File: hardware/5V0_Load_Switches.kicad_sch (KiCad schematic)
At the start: 28 parts, among them Q18 SI2302DDS-T1-GE3, Q19 SI2302DDS-T1-GE3, Q20 SI2302DDS-T1-GE3, U1 LMV321RIYLT, U2 INA199C1DCKR, U3 INA199C1DCKR, U4 INA199C1DCKR, U5 NVTFS5116PLTAG, U6 NVTFS5116PLTAG, U7 NVTFS5116PLTAG

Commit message: commit
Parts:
- R12, R13, R14: footprint (none) -> footprints:CRCW0603100KFKEAHP; symbol Device:R_US -> CRCW0603100KFKEAHP:CRCW0603100KFKEAHP; Arrow Part Number (none) -> CRCW0603100KFKEAHP; Arrow Price/Stock (none) -> https://www.arrow.com/en/products/crcw0603100kfkeahp/vishay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; Height (none) -> 0.55; Manufacturer_Name (none) -> Vishay; Manufacturer_Part_Number (none) -> CRCW0603100KFKEAHP; Mouser Part Number (none) -> 71-CRCW0603100KFKEAH; Mouser Price/Stock (none) -> https://www.mouser.co.uk/ProductDetail/Vishay-Dale/CRCW0603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
- R2: footprint (none) -> footprints:RC0805FR-0710KL; symbol Device:R_US -> RC0805FR-0710KL:RES
- R5: footprint (none) -> footprints:WSL2010R0200FEA; symbol Device:R_US -> WSL2010R0200FEA:WSL2010R0200FEA; Arrow Part Number (none) -> WSL2010R0200FEA; Arrow Price/Stock (none) -> https://www.arrow.com/en/products/wsl2010r0200fea/vishay; Manufacturer_Name (none) -> Vishay; Manufacturer_Part_Number (none) -> WSL2010R0200FEA; Mouser Part Number (none) -> 71-WSL2010R0200FEA; Mouser Price/Stock (none) -> https://www.mouser.co.uk/ProductDetail/Vishay-Dale/WSL2010R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
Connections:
- net +5V: now also R5.1; no longer R5.2
- net GND: now also R12.1, R13.1, R14.1; no longer R12.2, R13.2, R14.2, R2.1
- net at R1.1, U1.3 (+): no longer R2.2
- net at R8.1, U4.5 (IN-), U7.1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: now also R5.2; no longer R5.1
- net at Q20.1 (G), R10.2: now also R13.2; no longer R13.1
- net at Q18.1 (G), R11.2: now also R14.2; no longer R14.1
- net at Q19.1 (G), R9.2: now also R12.2; no longer R12.1
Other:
- moved on the sheet: R12, R13, R14, R2, R5

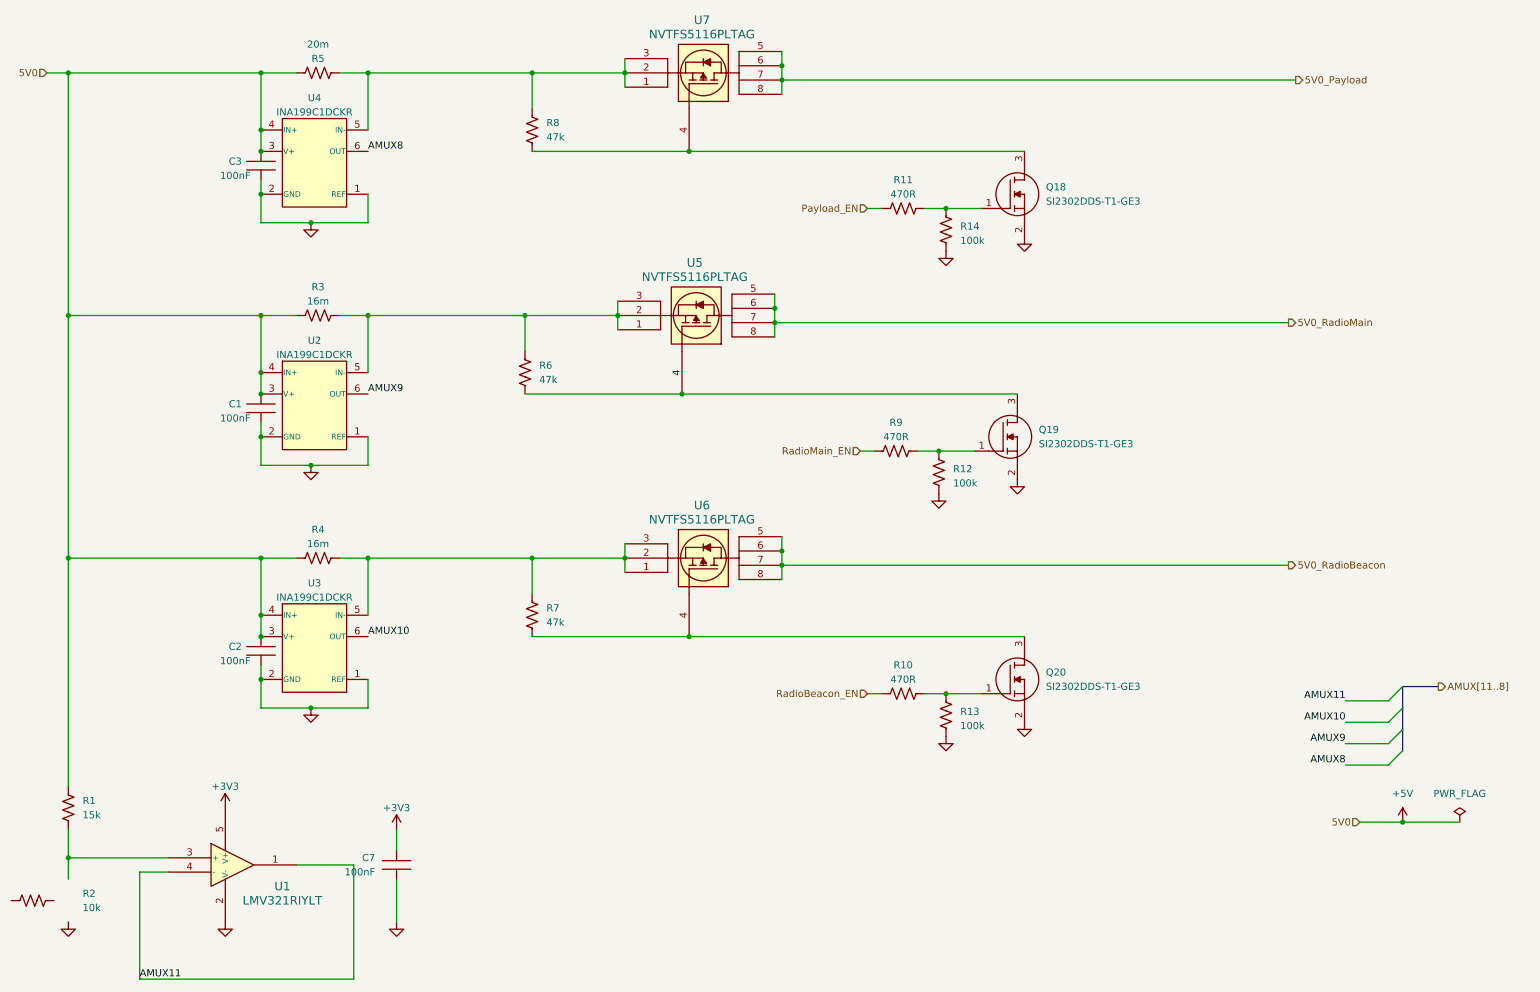
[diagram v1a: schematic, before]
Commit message: hardware: update in footprints
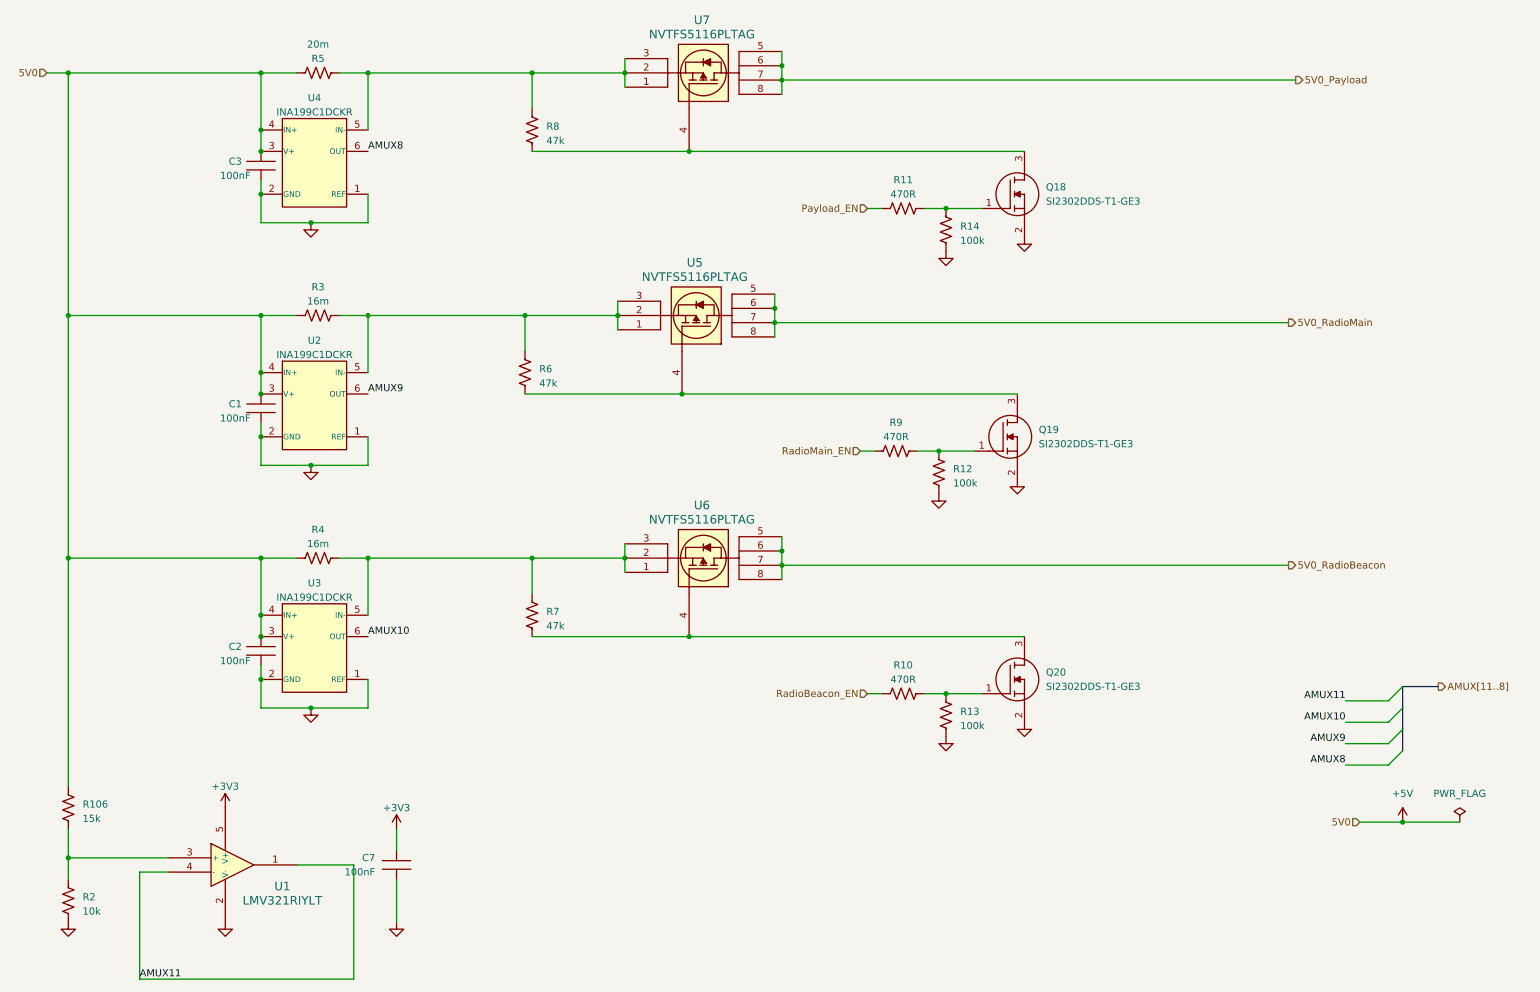
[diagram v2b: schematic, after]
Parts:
- removed R1: 15k, symbol Device:R_US
- added R106: 15k, footprints:CRCW060315K0FKEAHP, symbol CRCW060315K0FKEAHP:CRCW060315K0FKEAHP
- R10, R11, R9: footprint (none) -> footprints:CRCW0603470RFKEAHP; symbol Device:R_US -> CRCW0603470RFKEAHP:CRCW0603470RFKEAHP; automotive (none) -> Yes; automotive grade (none) -> Grade 0; category (none) -> Res; composition (none) -> Thick Film; device class L1 (none) -> Passive Components; device class L2 (none) -> Resistors; device class L3 (none) -> Chip SMD Resistors; height (none) -> 0.55mm; ipc land pattern name (none) -> RESC16085X45; lead free (none) -> Yes; library id (none) -> 3843bba7e74bf2ed; manufacturer (none) -> Vishay; package (none) -> 0603; power (none) -> 250mW; power rating (none) -> 0.33W; resistance (none) -> 470Ω; rohs (none) -> Yes; series (none) -> CRCW-HP e3; temperature coefficient (none) -> 100ppm/°C; temperature range high (none) -> +155°C; temperature range low (none) -> -55°C; tolerance (none) -> 1%; voltage rating (none) -> 75V
- R6, R7, R8: footprint (none) -> footprints:CRCW060347K0FKEAHP; symbol Device:R_US -> CRCW060347K0FKEAHP:CRCW060347K0FKEAHP; automotive (none) -> Yes; automotive grade (none) -> Grade 0; category (none) -> Res; composition (none) -> Thick Film; device class L1 (none) -> Passive Components; device class L2 (none) -> Resistors; device class L3 (none) -> Chip SMD Resistors; height (none) -> 0.55mm; ipc land pattern name (none) -> RESC16085X45; lead free (none) -> Yes; library id (none) -> 41c6336701360bfc; manufacturer (none) -> Vishay; package (none) -> 0603; power (none) -> 250mW; power rating (none) -> 0.33W; resistance (none) -> 47kΩ; rohs (none) -> Yes; series (none) -> CRCW-HP e3; temperature coefficient (none) -> 100ppm/°C; temperature range high (none) -> +155°C; temperature range low (none) -> -55°C; tolerance (none) -> 1%; voltage rating (none) -> 75V
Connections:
- net +5V: now also R106.2
- net GND: now also R2.2
- net Payload_EN: now also R11.2; no longer R11.1
- net RadioBeacon_EN: now also R10.2; no longer R10.1
- net RadioMain_EN: now also R9.2; no longer R9.1
- net at R4.1, U3.5 (IN-), U6.1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: now also R7.2; no longer R7.1
- net at Q20.3 (D), U6.4: now also R7.1; no longer R7.2
- net at R3.1, U2.5 (IN-), U5.1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: now also R6.2; no longer R6.1
- net at U1.3 (+): now also R2.1, R106.1
- net at Q19.3 (D), U5.4: now also R6.1; no longer R6.2
- net at R5.2, U4.5 (IN-), U7.1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: now also R8.2; no longer R8.1
- net at Q18.3 (D), U7.4: now also R8.1; no longer R8.2
- net at Q20.1 (G), R13.2: now also R10.1; no longer R10.2
- net at Q18.1 (G), R14.2: now also R11.1; no longer R11.2
- net at Q19.1 (G), R12.2: now also R9.1; no longer R9.2
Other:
- moved on the sheet: R10, R11, R2, R6, R7, R8, R9

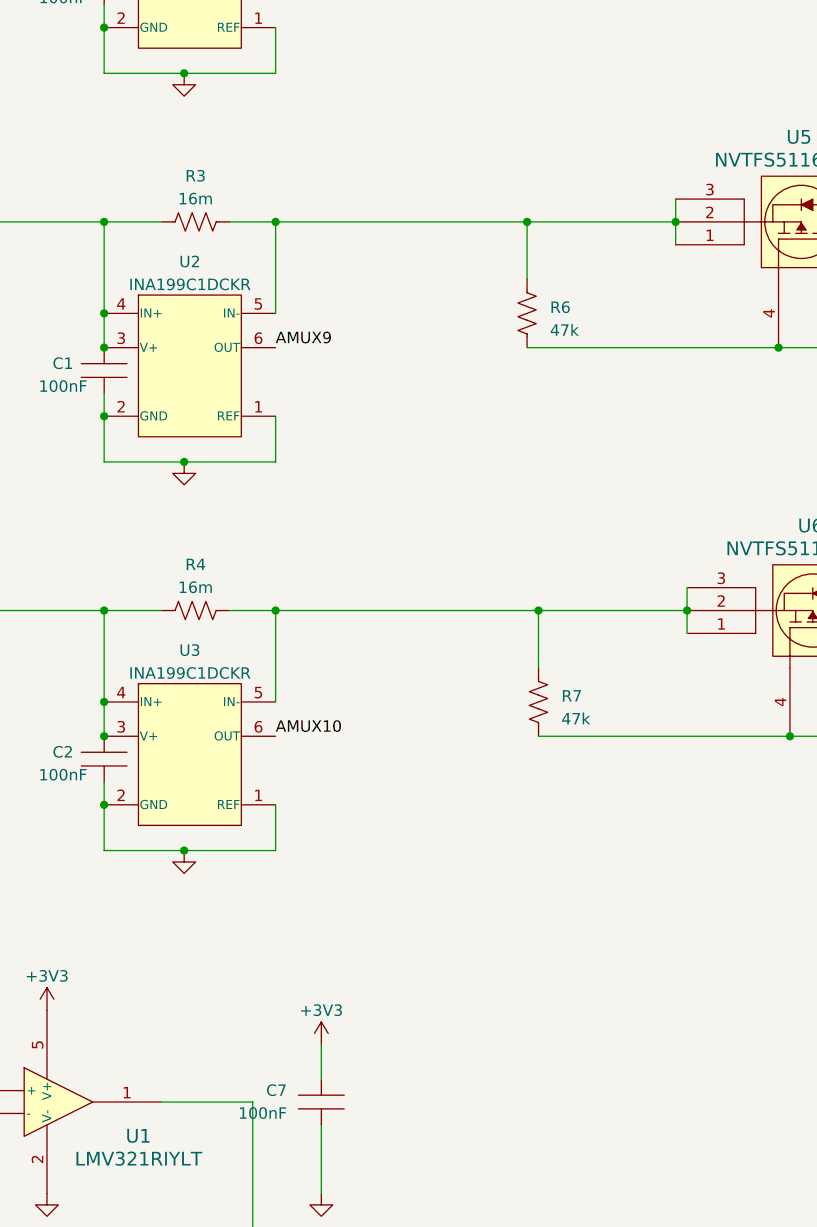
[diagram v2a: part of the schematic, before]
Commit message: hardware: All resistors added.
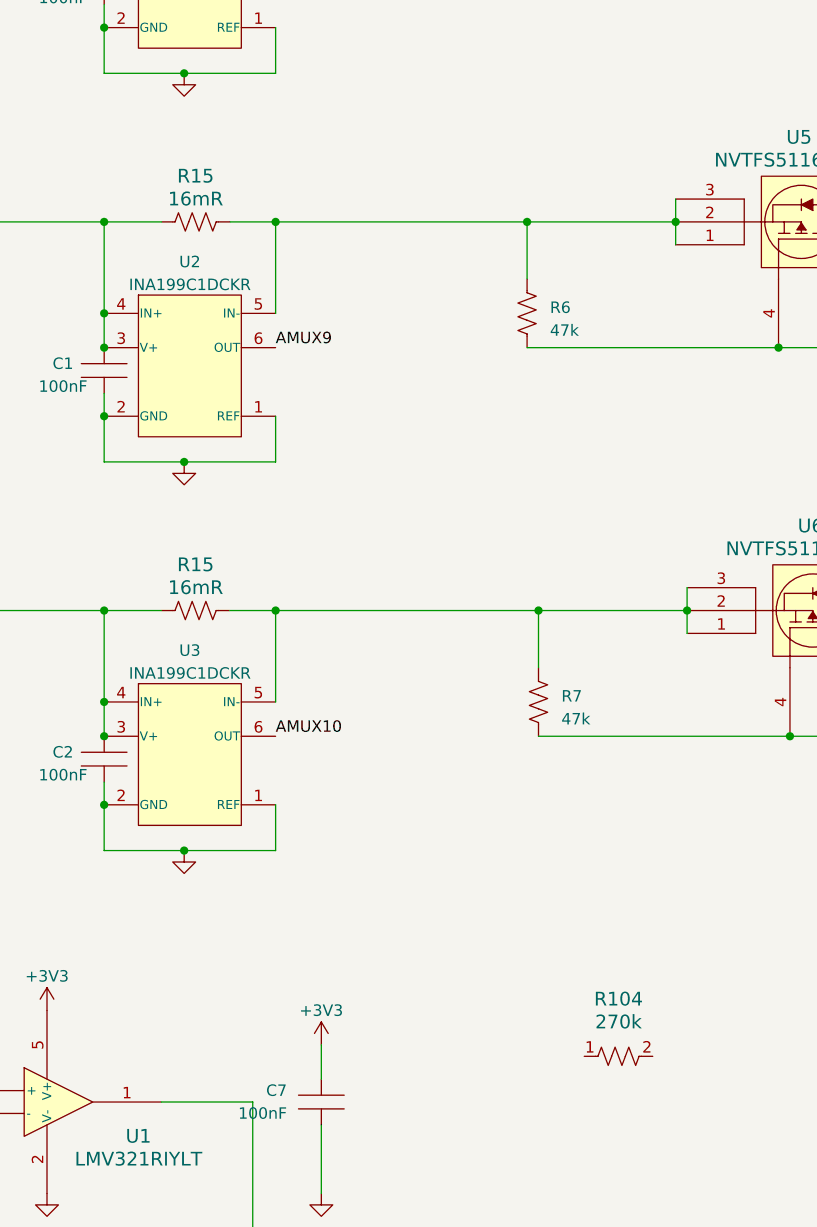
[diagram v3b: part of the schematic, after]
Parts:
- removed R3, R4: 16m, symbol Device:R_US
- added R104: 270k, RES_CRCW_0805_VIS, symbol CRCW0805270KFKEAHP:CRCW080520K0FKEAHP
- added R15 (x2): 16mR, footprints:WSL2010R0330FEA, symbol WSL2010R0160FEA:WSL2010R0160FEA
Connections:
- net +5V: now also R15.1, R15.1
- net at R7.2, U3.5 (IN-), U6.1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: now also R15.2
- net at R6.2, U2.5 (IN-), U5.1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: now also R15.2
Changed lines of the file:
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@@
+    )
+  )
+  (symbol (lib_id "WSL2010R0160FEA:WSL2010R0160FEA") (at 60.96 115.57 0) (unit 1)
+    (in_bom yes) (on_board yes) (dnp no) (fields_autoplaced)
+    (property "Reference" "R15" (at 67.31 110.49 0)
+      (effects (font (size 1.524 1.524)))
+    )
+    (property "Value" "16mR" (at 67.31 113.03 0)
+      (effects (font (size 1.524 1.524)))
+    )
+    (property "Footprint" "footprints:WSL2010R0330FEA" (at 64.77 125.73 0)
+      (effects (font (size 1.27 1.27) italic) hide)
+    )
+    (property "Datasheet" "WSL2010R0330FEA" (at 66.04 123.19 0)
+      (effects (font (size 1.27 1.27) italic) hide)
+    )
+    (pin "1")
+    (pin "2")
+    (instances
+      (project "eps-re_project"
+        (path "/2eebaa11-d7ed-4bfd-bc8e-988f68654d29/b2d6a676-b7d9-423e-8a54-05279452700b"
+          (reference "R15") (unit 1)
+        )
+        (path "/2eebaa11-d7ed-4bfd-bc8e-988f68654d29/4f028e55-4c46-47b6-9c45-f6b50d9d4db8"
+          (reference "R18") (unit 1)
+        )
+      )
     )
   )
@@
     )
   )
+  (symbol (lib_id "CRCW0805270KFKEAHP:CRCW080520K0FKEAHP") (at 107.95 163.83 0) (unit 1)
+    (in_bom yes) (on_board yes) (dnp no)
+    (property "Reference" "R104" (at 114.3 158.75 0)
+      (effects (font (size 1.524 1.524)))
+    )
+    (property "Value" "270k" (at 114.3 161.29 0)
+      (effects (font (size 1.524 1.524)))
+    )
+    (property "Footprint" "RES_CRCW_0805_VIS" (at 107.95 163.83 0)
+      (effects (font (size 1.27 1.27) italic) hide)
+    )
+    (property "Datasheet" "CRCW0805270KFKEAHP" (at 107.95 163.83 0)
+      (effects (font (size 1.27 1.27) italic) hide)
+    )
+    (pin "1")
+    (pin "2")
+    (instances
+      (project "eps-re_project"
+        (path "/2eebaa11-d7ed-4bfd-bc8e-988f68654d29/4f028e55-4c46-47b6-9c45-f6b50d9d4db8"
+          (reference "R104") (unit 1)
+        )
+      )
+    )
+  )
   (symbol (lib_id "C0603C104K5RACTU:C0603C104K5RACTU") (at 57.15 129.54 0) (unit 1)
     (in_bom yes) (on_board yes) (dnp no)
@@
     )
   )
+  (symbol (lib_id "WSL2010R0160FEA:WSL2010R0160FEA") (at 60.96 72.39 0) (unit 1)
+    (in_bom yes) (on_board yes) (dnp no) (fields_autoplaced)
+    (property "Reference" "R15" (at 67.31 67.31 0)
+      (effects (font (size 1.524 1.524)))
+    )
+    (property "Value" "16mR" (at 67.31 69.85 0)
+      (effects (font (size 1.524 1.524)))
+    )
+    (property "Footprint" "footprints:WSL2010R0330FEA" (at 64.77 82.55 0)
+      (effects (font (size 1.27 1.27) italic) hide)
+    )
+    (property "Datasheet" "WSL2010R0330FEA" (at 66.04 80.01 0)
+      (effects (font (size 1.27 1.27) italic) hide)
+    )
+    (pin "1")
+    (pin "2")
+    (instances
+      (project "eps-re_project"
+        (path "/2eebaa11-d7ed-4bfd-bc8e-988f68654d29/b2d6a676-b7d9-423e-8a54-05279452700b"
+          (reference "R15") (unit 1)
+        )
+        (path "/2eebaa11-d7ed-4bfd-bc8e-988f68654d29/4f028e55-4c46-47b6-9c45-f6b50d9d4db8"
+          (reference "R19") (unit 1)
+        )
+      )
+    )
+  )
   (symbol (lib_id "power:+3V3") (at 81.28 163.83 0) (unit 1)
     (in_bom yes) (on_board yes) (dnp no) (fields_autoplaced)
@@
     )
   )
-  (symbol (lib_id "Device:R_US") (at 67.31 72.39 270) (unit 1)
-    (in_bom yes) (on_board yes) (dnp no)
-    (property "Reference" "R3" (at 67.31 67.31 90)
-      (effects (font (size 1.27 1.27)))
-    )
-    (property "Value" "16m" (at 67.31 69.85 90)
-      (effects (font (size 1.27 1.27)))
-    )
-    (property "Footprint" "" (at 67.056 73.406 90)
-      (effects (font (size 1.27 1.27)) hide)
-    )
-    (property "Datasheet" "~" (at 67.31 72.39 0)
-      (effects (font (size 1.27 1.27)) hide)
-    )
-    (pin "1")
-    (pin "2")
-    (instances
-      (project "eps-re_project"
-        (path "/2eebaa11-d7ed-4bfd-bc8e-988f68654d29/b2d6a676-b7d9-423e-8a54-05279452700b"
-          (reference "R3") (unit 1)
-        )
-        (path "/2eebaa11-d7ed-4bfd-bc8e-988f68654d29/4f028e55-4c46-47b6-9c45-f6b50d9d4db8"
-          (reference "R18") (unit 1)
-        )
-      )
-      (project "EPS Analogico"
-        (path "/9af6272d-3cb8-4e37-b792-5888e300588f"
-          (reference "R1") (unit 1)
-        )
-      )
-    )
-  )
   (symbol (lib_id "INA199C1DCKR:INA199xxDCK") (at 44.45 58.42 0) (unit 1)
     (in_bom yes) (on_board yes) (dnp no)
@@
         )
       )
-    )
-  )
-  (symbol (lib_id "Device:R_US") (at 67.31 115.57 270) (unit 1)
-    (in_bom yes) (on_board yes) (dnp no)
-    (property "Reference" "R4" (at 67.31 110.49 90)
-      (effects (font (size 1.27 1.27)))
-    )
-    (property "Value" "16m" (at 67.31 113.03 90)
-      (effects (font (size 1.27 1.27)))
-    )
-    (property "Footprint" "" (at 67.056 116.586 90)
-      (effects (font (size 1.27 1.27)) hide)
-    )
-    (property "Datasheet" "~" (at 67.31 115.57 0)
-      (effects (font (size 1.27 1.27)) hide)
-    )
-    (pin "1")
-    (pin "2")
-    (instances
-      (project "eps-re_project"
-        (path "/2eebaa11-d7ed-4bfd-bc8e-988f68654d29/b2d6a676-b7d9-423e-8a54-05279452700b"
-          (reference "R4") (unit 1)
-        )
-        (path "/2eebaa11-d7ed-4bfd-bc8e-988f68654d29/4f028e55-4c46-47b6-9c45-f6b50d9d4db8"
-          (reference "R19") (unit 1)
-        )
-      )
-      (project "EPS Analogico"
-        (path "/9af6272d-3cb8-4e37-b792-5888e300588f"
-          (reference "R1") (unit 1)
-        )
-      )
